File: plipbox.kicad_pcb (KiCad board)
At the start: 2 copper layers, 10 parts, among them P1 PWR, P2 PARALLEL_PORT, P3 RS232, U1 MAX3221, U2 ARDUINO_NANO_V3

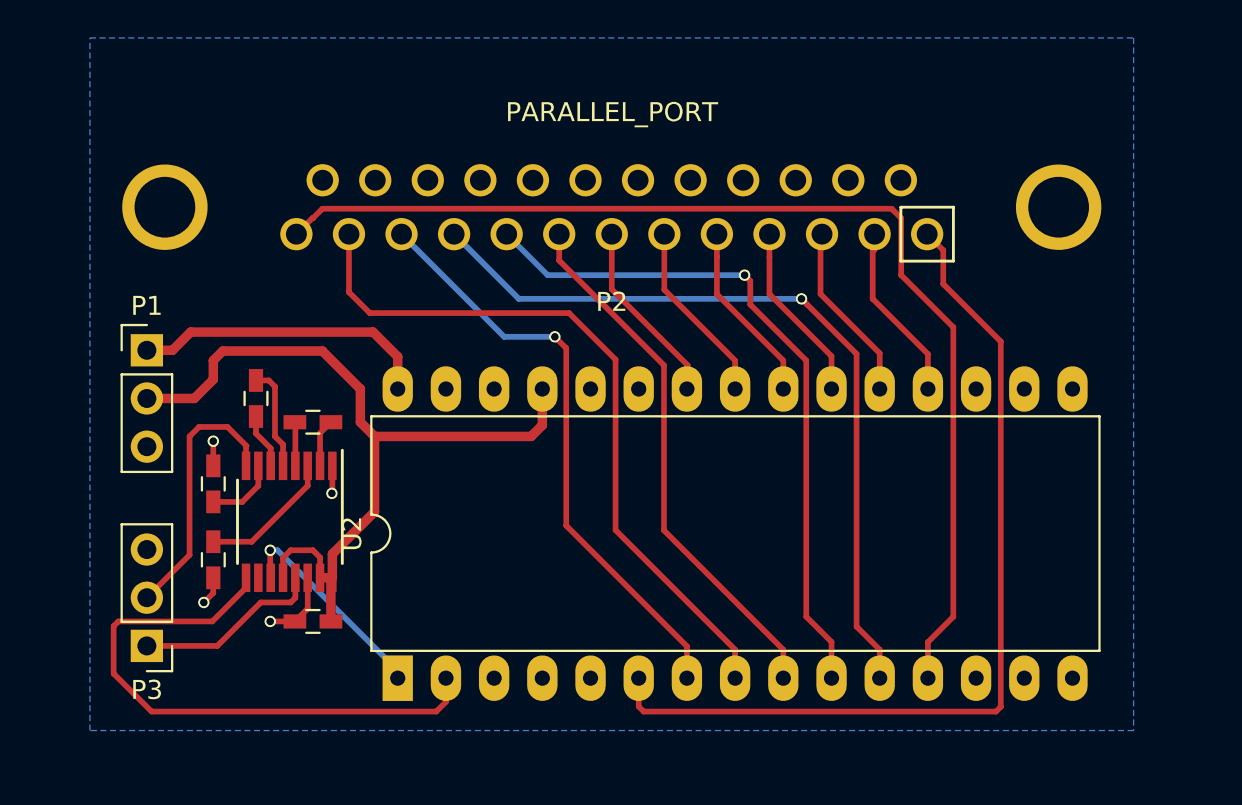
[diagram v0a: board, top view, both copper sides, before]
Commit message: Use edge connector, use MAX232 & other minor tweaks
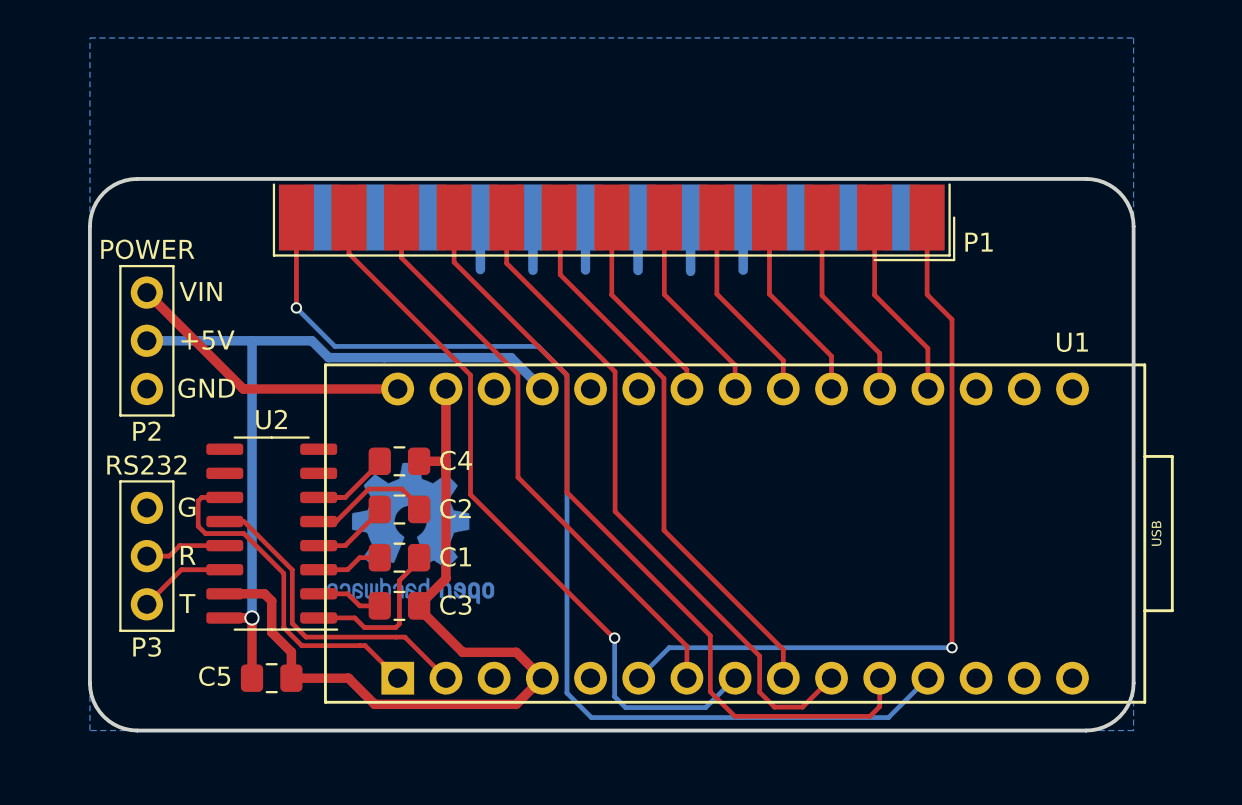
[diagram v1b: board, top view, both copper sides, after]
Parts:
- added V0: OSHW_LOGO, Symbol:OSHW-Logo2_9.8x8mm_Copper, B.Cu at (186.9, 113.6)
- C1: value 47n -> 1u; footprint Capacitors_SMD:C_0603_HandSoldering -> Capacitor_SMD:C_0805_2012Metric_Pad1.18x1.45mm_HandSolder
- C2: value 100n -> 1u; footprint Capacitors_SMD:C_0603_HandSoldering -> Capacitor_SMD:C_0805_2012Metric_Pad1.18x1.45mm_HandSolder
- C3, C4, C5: value 330n -> 1u; footprint Capacitors_SMD:C_0603_HandSoldering -> Capacitor_SMD:C_0805_2012Metric_Pad1.18x1.45mm_HandSolder
- P1: value PWR -> PARALLEL_PORT; footprint Pin_Headers:Pin_Header_Straight_1x03_Pitch2.54mm -> Connector_Dsub:DSUB-25_Male_EdgeMount_P2.77mm
- P2: value PARALLEL_PORT -> PWR; footprint kuro:DB25M-RA-TH -> plipbox:Pin_Header_Straight_1x03-ModSilkS
- P3: footprint Pin_Headers:Pin_Header_Straight_1x03_Pitch2.54mm -> plipbox:Pin_Header_Straight_1x03-ModSilkS
- U1: value MAX3221 -> ARDUINO_NANO_V3; footprint Housings_SSOP:TSSOP-16_4.4x5mm_Pitch0.65mm -> plipbox:Arduino_Nano_Socket
- U2: value ARDUINO_NANO_V3 -> MAX232; footprint Keio:DIP-30_W15.24mm_LongPads -> Package_SO:SOIC-16_3.9x9.9mm_P1.27mm
- moved U1 45.1 mm to (225.6, 113.6), turned to 90 degrees
- moved P1 25.5 mm to (197.5, 97.0), turned to 180 degrees
- moved P2 24.9 mm to (173.0, 100.9)
- moved C5 10.7 mm to (179.6, 121.2), turned to 0 degrees
- moved U2 10.1 mm to (179.6, 113.6), turned to 180 degrees
- moved C3 10.1 mm to (186.3, 117.4), turned to 0 degrees
- moved C1 8.47 mm to (186.3, 114.9)
- moved C4 8.25 mm to (186.3, 109.8), turned to 180 degrees
- moved C2 7.46 mm to (186.3, 112.3), turned to 0 degrees
- moved P3 2.19 mm to (173.0, 117.3)
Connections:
- C2 pad 1: /+5V -> Net-(C2-Pad1)
- C2 pad 2: GND -> Net-(C2-Pad2)
- C4 pad 1: Net-(C4-Pad1) -> GND
- C5 pad 1: Net-(C5-Pad1) -> /+5V
- P1 pad 1: /VIN -> /~STROBE
- P1 pad 2: /+5V -> /DATA0
- P1 pad 3: GND -> /DATA1
- P2 pad 1: /~STROBE -> /VIN
- P2 pad 2: /DATA0 -> /+5V
- P2 pad 3: /DATA1 -> GND
- U2 pad 1: /DIN -> Net-(C1-Pad1)
- U2 pad 10: /DATA7 -> (no net)
- U2 pad 11: /~ACK -> /DIN
- U2 pad 12: /SELECT -> /ROUT
- U2 pad 13: (no net) -> /RIN
- U2 pad 14: (no net) -> /DOUT
- U2 pad 15: (no net) -> GND
- U2 pad 16: (no net) -> /+5V
- U2 pad 2: /ROUT -> Net-(C3-Pad1)
- U2 pad 3: (no net) -> Net-(C1-Pad2)
- U2 pad 4: GND -> Net-(C2-Pad1)
- U2 pad 5: (no net) -> Net-(C2-Pad2)
- U2 pad 6: /~STROBE -> Net-(C4-Pad2)
- U2 pad 7: /BUSY -> (no net)
- U2 pad 8: /POUT -> (no net)
- U2 pad 9: /DATA6 -> (no net)
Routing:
- net GND: track 8.15 -> 60.3 mm, vias 4 -> 0
- net /ROUT: track 31.2 -> 16.7 mm
- net /RIN: track 14.1 -> 4.33 mm
- net /DIN: track 11.2 -> 18.4 mm, vias 1 -> 0
- net /~STROBE: track 47.3 -> 40.5 mm, vias 0 -> 1
- net Net-(C2-Pad2): track 0.00 -> 6.55 mm
- net Net-(C1-Pad1): track 2.54 -> 8.47 mm
- net Net-(C4-Pad1): track 5.49 -> 0.00 mm
- net /DOUT: track 9.93 -> 4.86 mm
- net Net-(C2-Pad1): track 0.00 -> 4.06 mm
- net Net-(C5-Pad1): track 3.78 -> 0.00 mm
- net Net-(C3-Pad1): track 7.25 -> 3.48 mm
- net Net-(C4-Pad2): track 2.92 -> 5.20 mm
- net /+5V: track 43.2 -> 41.0 mm, vias 0 -> 1
- net Net-(C1-Pad2): track 2.31 -> 3.69 mm
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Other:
- board outline added: 55 x 29.1 mm
- net class Power added: clearance 0.2, trace_width 0.5, via_dia 0.8, via_drill 0.6
- rule pad_to_mask_clearance: 0.2 -> 0
- board text added: "+5V"
- board text added: "G"
- board text added: "PLIPBOX REV. 1S By lallafa, kuro68k and SukkoPera Released under the GNU GPL v3"
- board text added: "POWER"
- board text added: "R"
- board text added: "T"

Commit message: Add diode and fix C3 C3 was WRONG in Rev.1S, it needs to be between pin 2 of U1 and VCC, not GND. The diode should only be mounted if the Amiga is modded so that power on the +5V line is not limited.
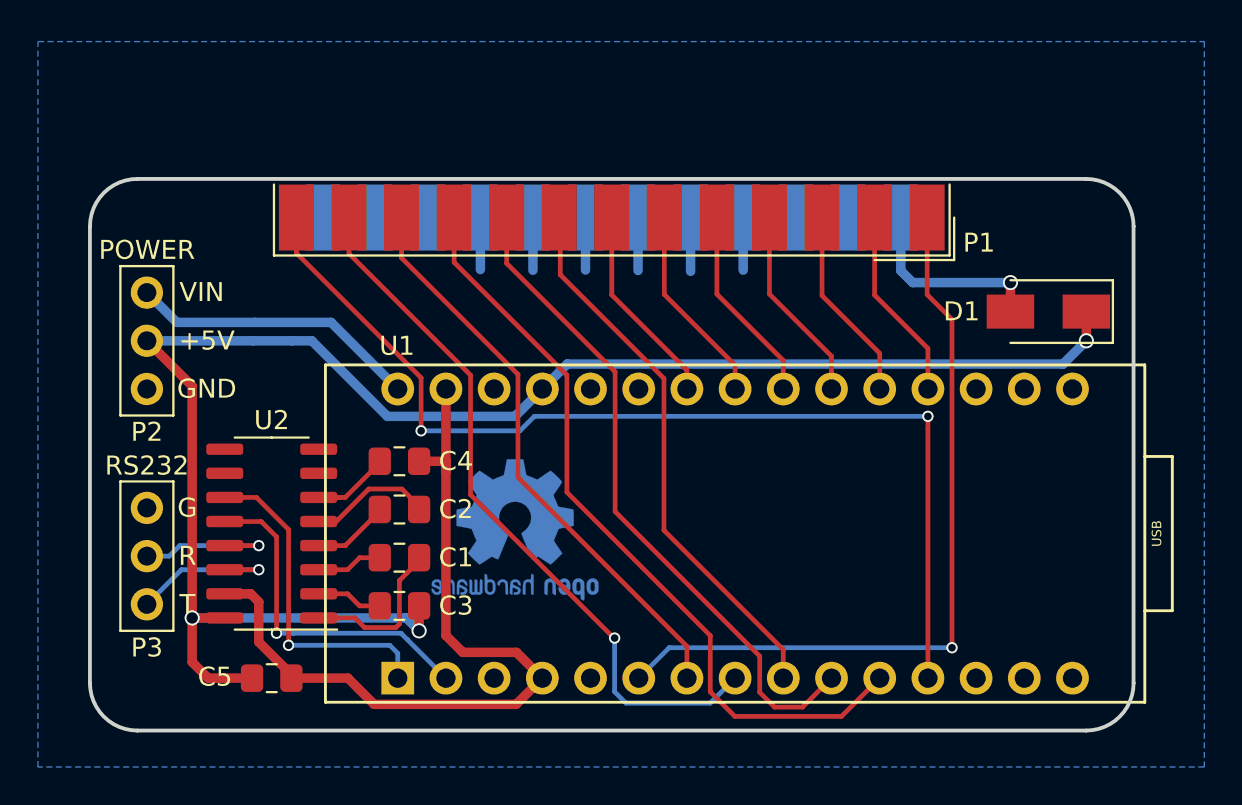
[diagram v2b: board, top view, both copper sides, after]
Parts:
- added D1: D, Diode_SMD:D_SMA, F.Cu at (220.5, 101.9)
- moved V0 5.51 mm to (192.4, 113.4)
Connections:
- C3 pad 2: GND -> +5V
- C5 pad 1: /+5V -> +5V
- P1 pad 14: (no net) -> Net-(D1-Pad2)
- P2 pad 2: /+5V -> +5V
- U1 pad 5V: /+5V -> +5V
- U2 pad 16: /+5V -> +5V
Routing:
- net +5V: track 0.00 -> 91.1 mm, vias 0 -> 3
- net /+5V: track 41.0 -> 0.00 mm, vias 1 -> 0
- net Net-(D1-Pad2): track 0.00 -> 10.4 mm, vias 0 -> 1
- net /DOUT: track 4.86 -> 8.51 mm, vias 0 -> 1
- net /RIN: track 4.33 -> 7.86 mm, vias 0 -> 1
- net /SELECT: track 57.7 -> 54.8 mm, vias 1 -> 2
- net GND: track 60.3 -> 58.8 mm
- net /ROUT: track 16.7 -> 18.1 mm, vias 0 -> 1
- net /DIN: track 18.4 -> 17.3 mm, vias 0 -> 1
- net /~ACK: track 41.8 -> 40.9 mm
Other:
- board text added: "PLIPBOX REV. 2S By lallafa, kuro68k and SukkoPera Released under the GNU GPL v3"
- board text removed: "1"
- board text removed: "5V"
- board text removed: "Arduino Nano V3"
- board text removed: "DB25M"
- board text removed: "PARALLEL PORT"
- board text removed: "PLIPBOX REV. 1S By lallafa, kuro68k and SukkoPera Released under the GNU GPL v3"
- board text removed: "RX"
- board text removed: "TX"
- board text removed: "plipbox by lallafa PCB/RS232 by kuro68k lallafa.de/blog/amiga-projects/plipbox/"

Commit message: Add reset jumper and ready for V2S
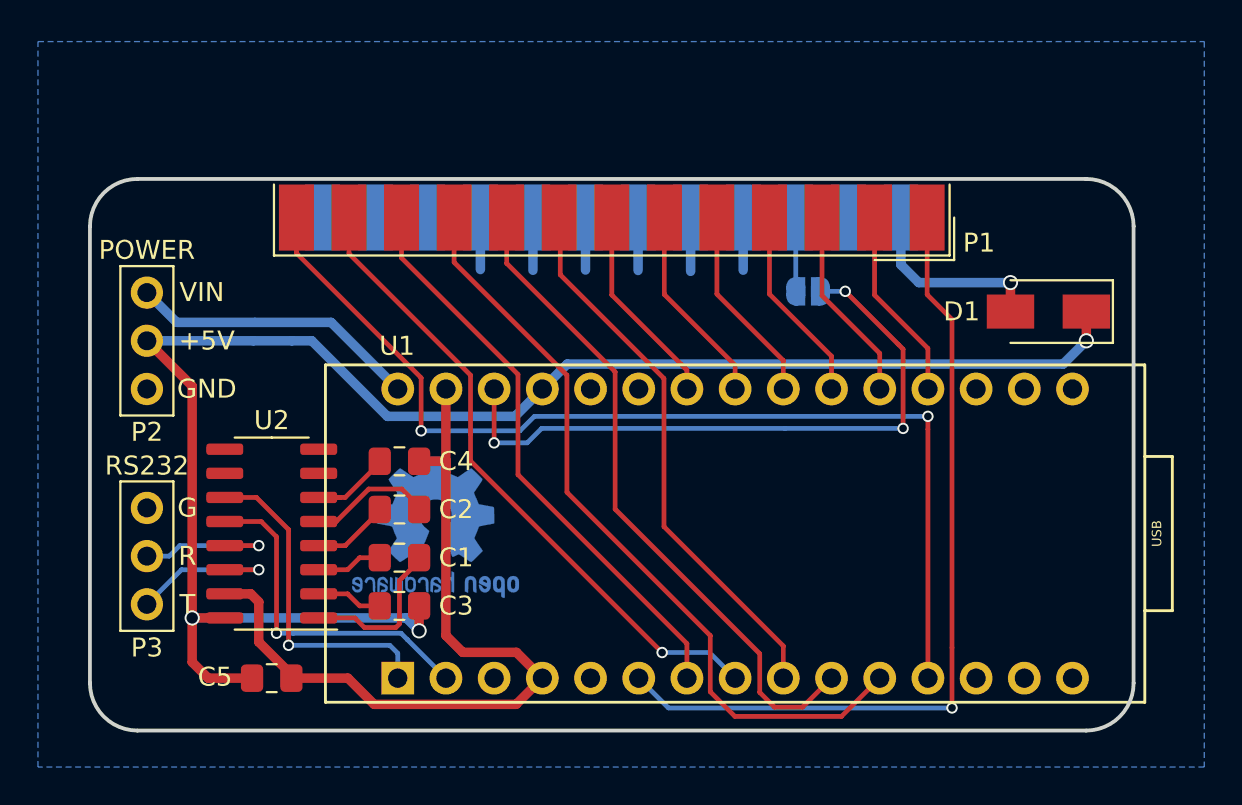
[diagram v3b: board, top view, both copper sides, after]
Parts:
- added JP1: JMP_RST, Jumper:SolderJumper-2_P1.3mm_Open_RoundedPad1.0x1.5mm, B.Cu at (207.8, 100.9)
- D1: value D -> 1n5819
- moved V0 4.19 mm to (188.2, 113.3)
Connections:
- P1 pad 15: (no net) -> Net-(P1-Pad15)
- P1 pad 16: (no net) -> /~RESET
- P1 pad 23: (no net) -> Net-(P1-Pad23)
- P1 pad 24: (no net) -> Net-(P1-Pad24)
- P1 pad 25: (no net) -> Net-(P1-Pad25)
- U1 pad 3V3: (no net) -> Net-(U1-Pad3V3)
- U1 pad A6: (no net) -> Net-(U1-PadA6)
- U1 pad A7: (no net) -> Net-(U1-PadA7)
- U1 pad AREF: (no net) -> Net-(U1-PadAREF)
- U1 pad D10: (no net) -> Net-(U1-PadD10)
- U1 pad D11: (no net) -> Net-(U1-PadD11)
- U1 pad D12: (no net) -> Net-(U1-PadD12)
- U1 pad D13: (no net) -> Net-(U1-PadD13)
- U1 pad D2: (no net) -> Net-(U1-PadD2)
- U1 pad RST1: (no net) -> Net-(U1-PadRST1)
- U1 pad RST2: (no net) -> Net-(JP1-Pad1)
- U2 pad 10: (no net) -> Net-(U2-Pad10)
- U2 pad 7: (no net) -> Net-(U2-Pad7)
- U2 pad 8: (no net) -> Net-(U2-Pad8)
- U2 pad 9: (no net) -> Net-(U2-Pad9)
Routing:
- net Net-(JP1-Pad1): track 0.00 -> 34.5 mm, vias 0 -> 3
- net /POUT: track 37.9 -> 34.2 mm
- net /~RESET: track 0.00 -> 3.28 mm
- net /~STROBE: track 40.5 -> 43.6 mm
